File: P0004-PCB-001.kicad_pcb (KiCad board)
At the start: 2 copper layers, 100 x 100 mm, 5 parts

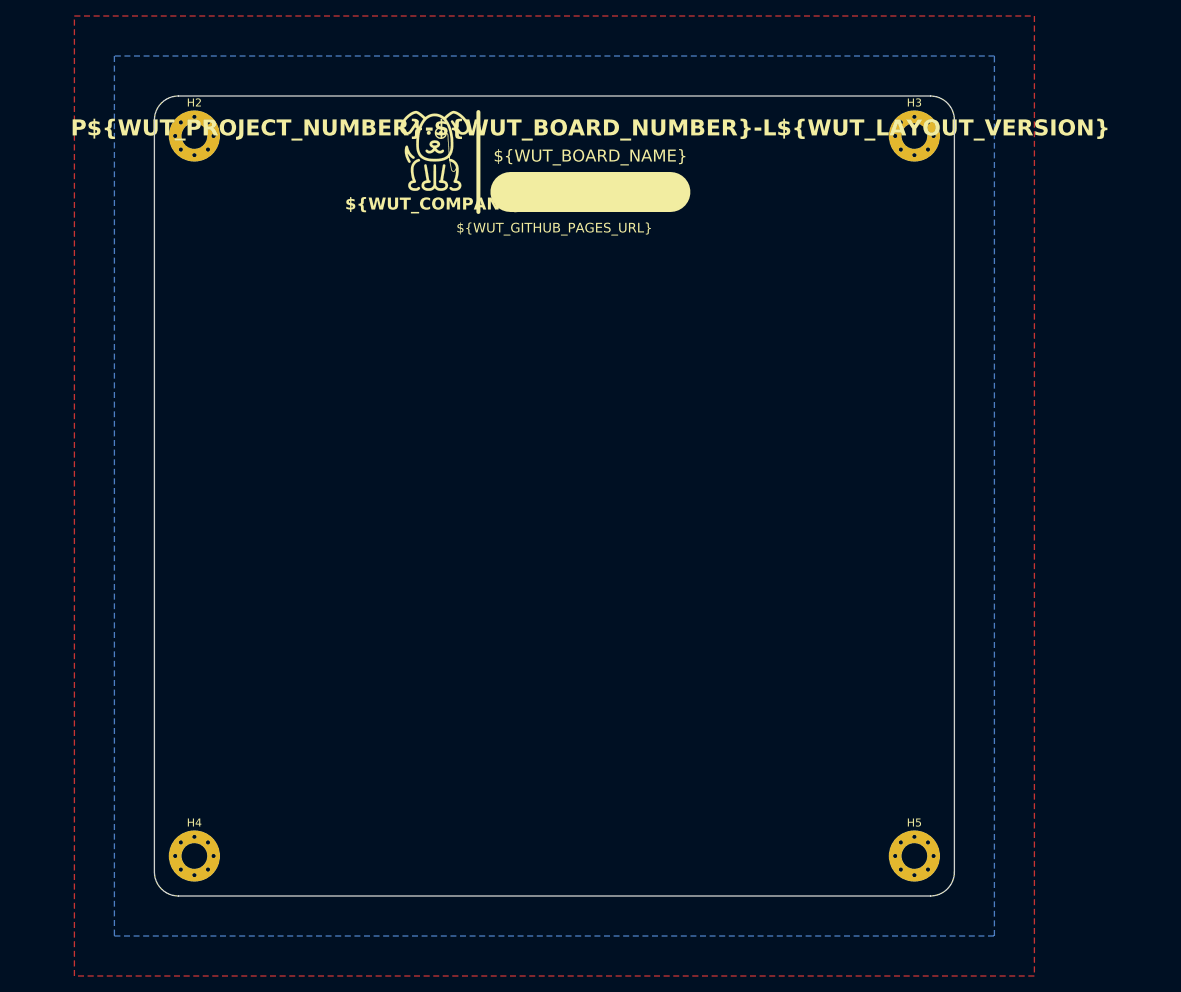
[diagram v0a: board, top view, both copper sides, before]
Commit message: started adding components
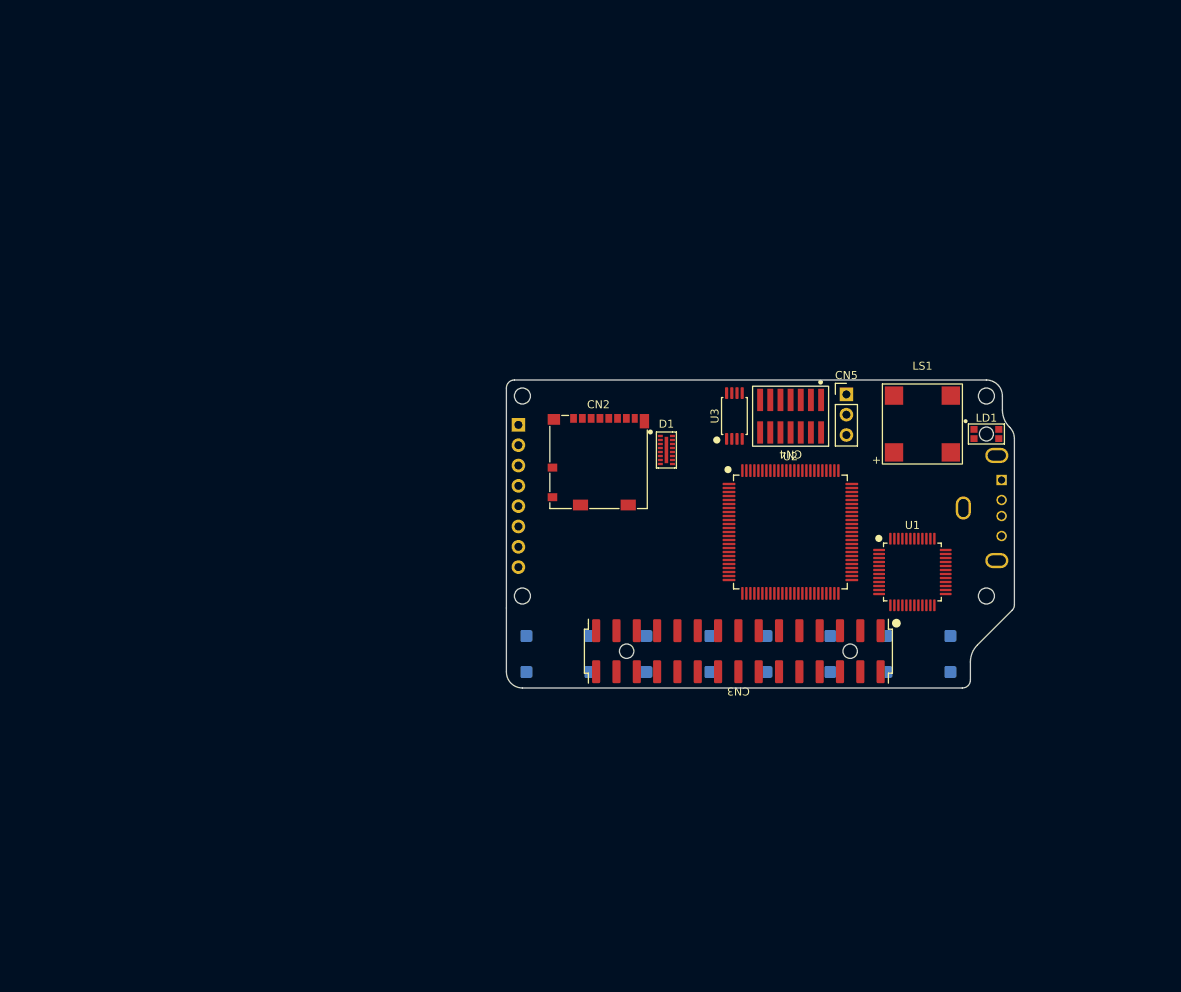
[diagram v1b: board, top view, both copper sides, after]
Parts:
- added CN1: Molex 105057-0001, Connector_WUT:USB-A_Molex_105057-0001_TH_Vertical, B.Cu at (204.0, 101.5)
- added CN2: 104031-0811, Connector_WUT:microSD_HC_Molex_104031-0811, F.Cu at (155.5, 95.8)
- added CN3: Liansheng PH--00603, Connector_WUT:Liansheng_PH--00603, F.Cu at (173.0, 119.4)
- added CN4: Samtec FTSH-107-01-L-DV-K, Connector_WUT:Header_Samtec_FTSH-107-01-L-DV-K, F.Cu at (179.5, 90.0)
- added CN5: M20-9990346, Connector_WUT:PinHeader_1x03_P2.54mm_Vertical, F.Cu at (186.5, 87.3)
- added D1: ECLAMP2410P, Diode_WUT:Semtech_ECLAMP2410P, F.Cu at (164.0, 94.2)
- added H10: M2x5mm, Accessories_WUT:Accu_HPS-4-2.2-5-POM-BL, B.Cu at (146.0, 87.5)
- added H11: M2x5mm, Accessories_WUT:Accu_HPS-4-2.2-5-POM-BL, B.Cu at (204.0, 112.5)
- added H12: M2x5mm, Accessories_WUT:Accu_HPS-4-2.2-5-POM-BL, B.Cu at (146.0, 112.5)
- added H13: ~, Misc_WUT:Logo_10mmx10mm, B.Cu at (189.5, 96.8)
- added H6: M2x2mm, Accessories_WUT:Accu_HPS-4-2.2-2-POM-BL, B.Cu at (146.0, 87.5)
- added H7: M2x2mm, Accessories_WUT:Accu_HPS-4-2.2-2-POM-BL, B.Cu at (204.0, 112.5)
- added H8: M2x2mm, Accessories_WUT:Accu_HPS-4-2.2-2-POM-BL, B.Cu at (146.0, 112.5)
- added H9: M2x5mm, Accessories_WUT:Accu_HPS-4-2.2-5-POM-BL, B.Cu at (204.0, 87.5)
- added LD1: Wuerth 156125M173000, LED_WUT:Wuerth_156125M173000, F.Cu at (204.0, 92.2)
- added LS1: HNDZ MLT8530, Audio_WUT:HNDZ_MLT8530, F.Cu at (196.0, 91.0)
- added SW1: Khon TSA06131-100B332CA, Switch_WUT:Khon_TSB06331-090, B.Cu at (195.5, 119.8)
- added SW2: Khon TSA06131-100B332CA, Switch_WUT:Khon_TSB06331-090, B.Cu at (180.5, 119.8)
- added SW3: Khon TSA06131-100B332CA, Switch_WUT:Khon_TSB06331-090, B.Cu at (165.5, 119.8)
- added SW4: Khon TSA06131-100B332CA, Switch_WUT:Khon_TSB06331-090, B.Cu at (150.5, 119.8)
- added U1: W5500, IC_WUT:LQFP-48_7x7mm_P0.5mm, F.Cu at (194.8, 109.5)
- added U2: STM32H743VIT6, IC_WUT:LQFP-100_14x14mm_P0.5mm, F.Cu at (179.5, 104.5)
- added U3: Microchip 24AA256UIDT-I/ST, IC_WUT:TSSOP-8_4.4x3mm_P0.65mm, F.Cu at (172.5, 90.0)
- added ZF1: East Rising ER-TFTM019-1-SPI, Display_WUT:East-Rising_ER-TFTM019-1-SPI, B.Cu at (173.0, 100.0)
- H1: value ~ -> Khon SC109AM1; footprint Misc_WUT:Logo_10mmx10mm -> Switch_WUT:Khon_SC109; moved to B.Cu
- H2, H3, H4: value M3 with vias -> Khon SC109AM1; footprint MountingHole:MountingHole_3.2mm_M3_Pad_Via -> Switch_WUT:Khon_SC109; moved to B.Cu
- H5: value M3 with vias -> M2x2mm; footprint MountingHole:MountingHole_3.2mm_M3_Pad_Via -> Accessories_WUT:Accu_HPS-4-2.2-2-POM-BL; moved to B.Cu
- moved H2 99.5 mm to (180.5, 119.8), turned to 180 degrees
- moved H1 87.2 mm to (195.5, 119.8), turned to 180 degrees
- moved H3 71.2 mm to (165.5, 119.8), turned to 180 degrees
- moved H5 58.2 mm to (204.0, 87.5), turned to 180 degrees
- moved H4 52.0 mm to (150.5, 119.8), turned to 180 degrees
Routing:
- removed copper zone on B.Cu, net 0V
- removed copper zone on F.Cu, net 0V
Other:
- board size 100 x 100 mm -> 63.5 x 38.5 mm
- board text added: "Hammond 1455K1201"
- board text added: "JLCMC K143-15244-H6-L150"
- board text added: "Light pipe: PLPC2-375"

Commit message: testing ci config
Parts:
- SW1, SW2, SW3, SW4: value Khon TSA06131-100B332CA -> Khon TSB06331-090D332DA-R0500

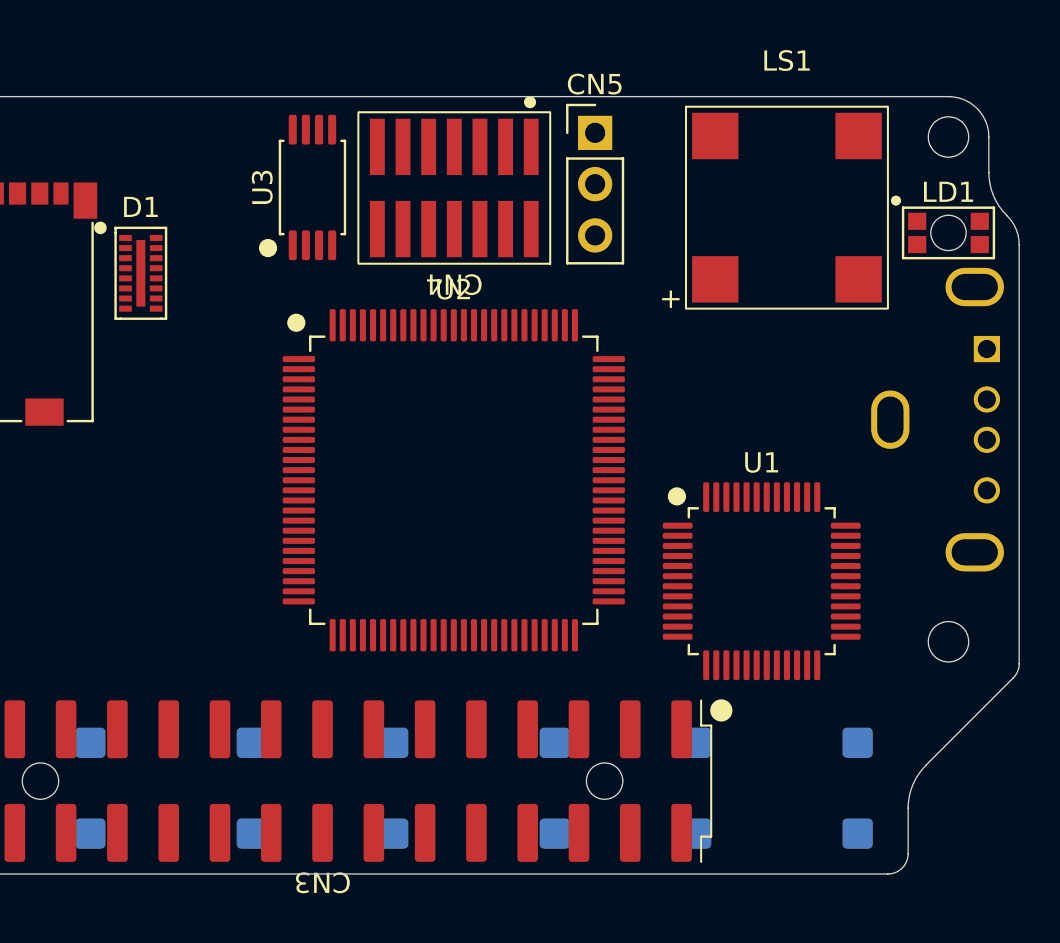
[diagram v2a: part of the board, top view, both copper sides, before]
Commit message: started on DCDC section
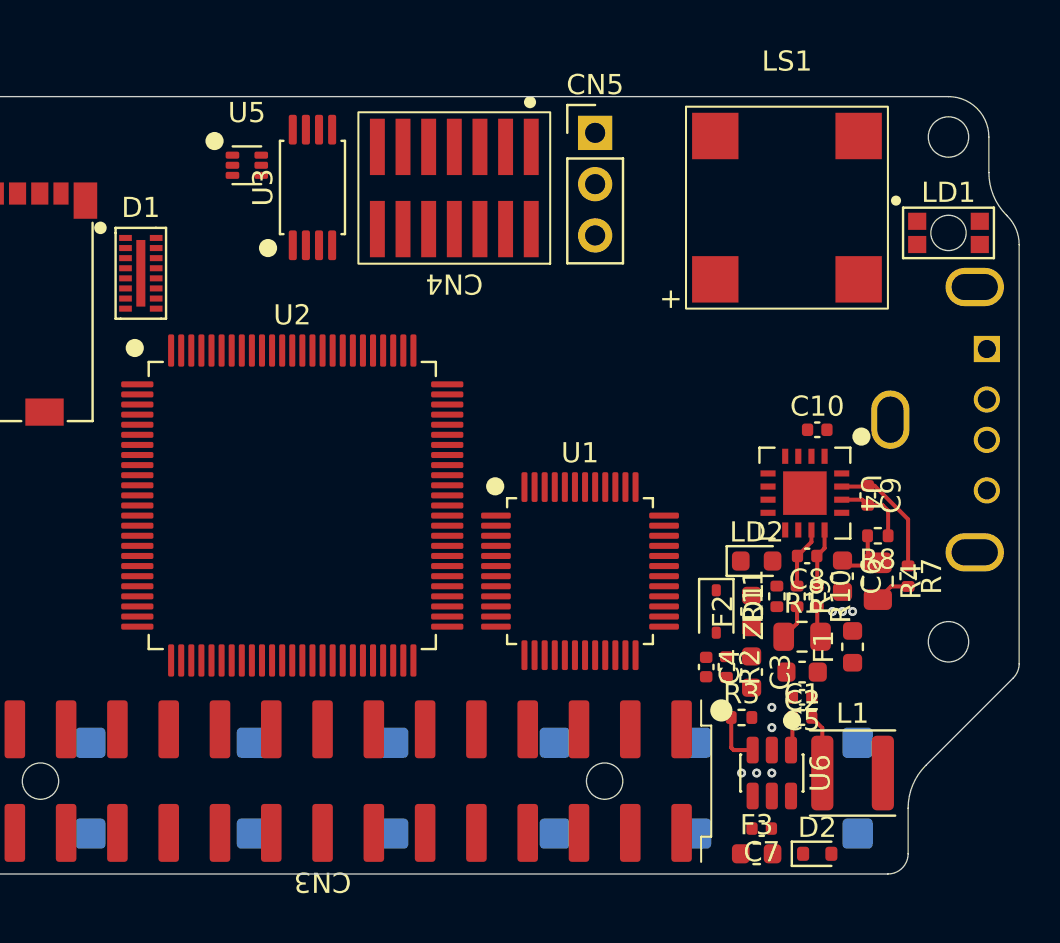
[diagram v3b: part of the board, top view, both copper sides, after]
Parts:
- added C1: 100n, Capacitor_WUT:C_0402_1005Metric, F.Cu at (196.8, 116.2)
- added C10: 100n, Capacitor_WUT:C_0402_1005Metric, F.Cu at (197.5, 102.0)
- added C2: 22u, Capacitor_SMD:C_0603_1608Metric, F.Cu at (196.8, 114.0)
- added C3: 22u, Capacitor_SMD:C_0603_1608Metric, F.Cu at (194.2, 114.0)
- added C4: 15p, Capacitor_WUT:C_0402_1005Metric, F.Cu at (192.0, 113.8)
- added C5: 100n, Capacitor_WUT:C_0402_1005Metric, F.Cu at (196.8, 115.2)
- added C6: 22u, Capacitor_SMD:C_0603_1608Metric, F.Cu at (198.8, 109.2)
- added C7: 2u2, Capacitor_WUT:C_0402_1005Metric, F.Cu at (194.8, 121.8)
- added C8: 100n, Capacitor_WUT:C_0402_1005Metric, F.Cu at (197.0, 108.2)
- added C9: 100n, Capacitor_WUT:C_0402_1005Metric, F.Cu at (200.0, 105.2)
- added D2: 15V, Diode_SMD:D_SOD-523, F.Cu at (197.5, 123.0)
- added F1: 250mA, Fuse:Fuse_0603_1608Metric, F.Cu at (199.2, 112.8)
- added F2: 1A, Fuse:Fuse_0603_1608Metric, F.Cu at (194.2, 111.0)
- added F3: 1A, Fuse:Fuse_0603_1608Metric, F.Cu at (194.5, 123.0)
- added L1: 10u, Inductor_WUT:APV_ANR4030, F.Cu at (199.2, 119.0)
- added LD2: Green, LED_SMD:LED_0603_1608Metric, F.Cu at (194.5, 108.5)
- added R1: 150m, Resistor_SMD:R_0805_2012Metric, F.Cu at (196.8, 112.2)
- added R10: 100R, Resistor_WUT:R_0402_1005Metric, F.Cu at (197.5, 110.2)
- added R11: 1k0, Resistor_WUT:R_0402_1005Metric, F.Cu at (195.5, 110.2)
- added R2: 47k, Resistor_WUT:R_0402_1005Metric, F.Cu at (193.0, 113.8)
- added R3: 15k, Resistor_WUT:R_0402_1005Metric, F.Cu at (193.8, 116.2)
- added R4: 150m, Resistor_SMD:R_0805_2012Metric, F.Cu at (200.5, 109.5)
- added R7: 100R, Resistor_WUT:R_0402_1005Metric, F.Cu at (202.0, 109.2)
- added R8: 100R, Resistor_WUT:R_0402_1005Metric, F.Cu at (200.5, 107.2)
- added R9: 100R, Resistor_WUT:R_0402_1005Metric, F.Cu at (196.5, 110.2)
- added U4: INA3221AIRGV, IC_WUT:Texas_VQFN-16-1EP_RGV0016A, F.Cu at (196.9, 105.1)
- added U5: TMP102AIDRL, IC_WUT:SOT-563, F.Cu at (169.2, 88.9)
- added U6: TI LMR54410DBV, IC_WUT:SOT-23-6, F.Cu at (195.2, 119.0)
- added ZD1: 3V3, Diode_SMD:D_SOD-323, F.Cu at (192.5, 111.0)
- moved U1 9.01 mm to (185.8, 109.0)
- moved U2 8.10 mm to (171.5, 105.8)
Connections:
- U2 pad 10: Net-(U2-VSS-Pad10) -> unconnected-(U2-VSS-Pad10)
- U2 pad 26: Net-(U2-VSS-Pad10) -> unconnected-(U2-VSS-Pad26)
- U2 pad 49: Net-(U2-VSS-Pad10) -> unconnected-(U2-VSS-Pad49)
- U2 pad 74: Net-(U2-VSS-Pad10) -> unconnected-(U2-VSS-Pad74)
- U2 pad 99: Net-(U2-VSS-Pad10) -> unconnected-(U2-VSS-Pad99)
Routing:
- net /Power Supplies/3V3_EXPANSION_SENSE_P: track 0.00 -> 6.30 mm
- net /Power Supplies/3V3_EXPANSION_SENSE_N: track 0.00 -> 3.76 mm
- net /Power Supplies/3V3_EXPANSION: track 0.00 -> 3.36 mm
- net /Power Supplies/VINT_SENSE_N: track 0.00 -> 3.07 mm
- net /Power Supplies/SW: track 0.00 -> 2.97 mm
- net /Power Supplies/VINT_SENSE_P: track 0.00 -> 2.94 mm
- net Net-(U6-FB): track 0.00 -> 2.60 mm
- net Net-(F1-Pad2): track 0.00 -> 1.77 mm
- net Net-(C3-Pad1): track 0.00 -> 1.76 mm
- net Net-(U6-CB): track 0.00 -> 1.74 mm
- net /Power Supplies/VOUT: track 0.00 -> 1.56 mm
- net 0V: vias 0 -> 8
